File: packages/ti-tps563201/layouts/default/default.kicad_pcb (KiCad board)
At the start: 2 copper layers, 12 parts

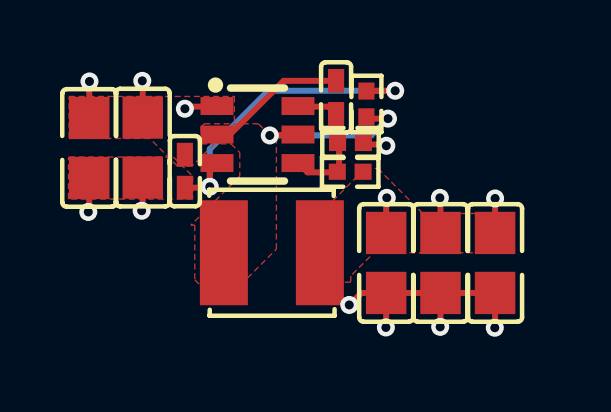
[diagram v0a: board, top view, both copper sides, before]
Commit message: fixing up tps564201
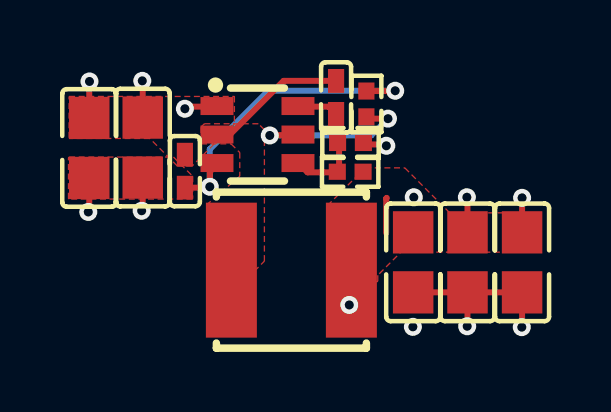
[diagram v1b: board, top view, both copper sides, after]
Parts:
- L1: value 2.2µH ±20% 4.3A 48mΩ -> 2.2µH ±20% 3.1A 42mΩ; footprint Sunlord_WPN4020H2R2MT:IND-SMD_L4.0-W4.0 -> cjiang_FNR5020S2R2MT:IND-SMD_L5.0-W5.0_FNR5012S
- moved C5 0.90 mm to (187.0, 99.8)
- moved C7 0.90 mm to (183.4, 99.8)
- moved C6 0.90 mm to (185.2, 99.8)
- moved L1 0.87 mm to (179.3, 100.1), turned to 0 degrees
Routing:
- net GND: track 12.8 -> 10.2 mm, vias 8 -> 7
- net power-VCC: vias 3 -> 4

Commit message: layout tidy
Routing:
- net power-VCC: track 3.51 -> 2.33 mm
- net GND: track 10.2 -> 11.4 mm
